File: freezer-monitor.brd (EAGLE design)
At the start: 50.8 x 22.9 mm, 7 parts, among them J1 1X2-3.5MM

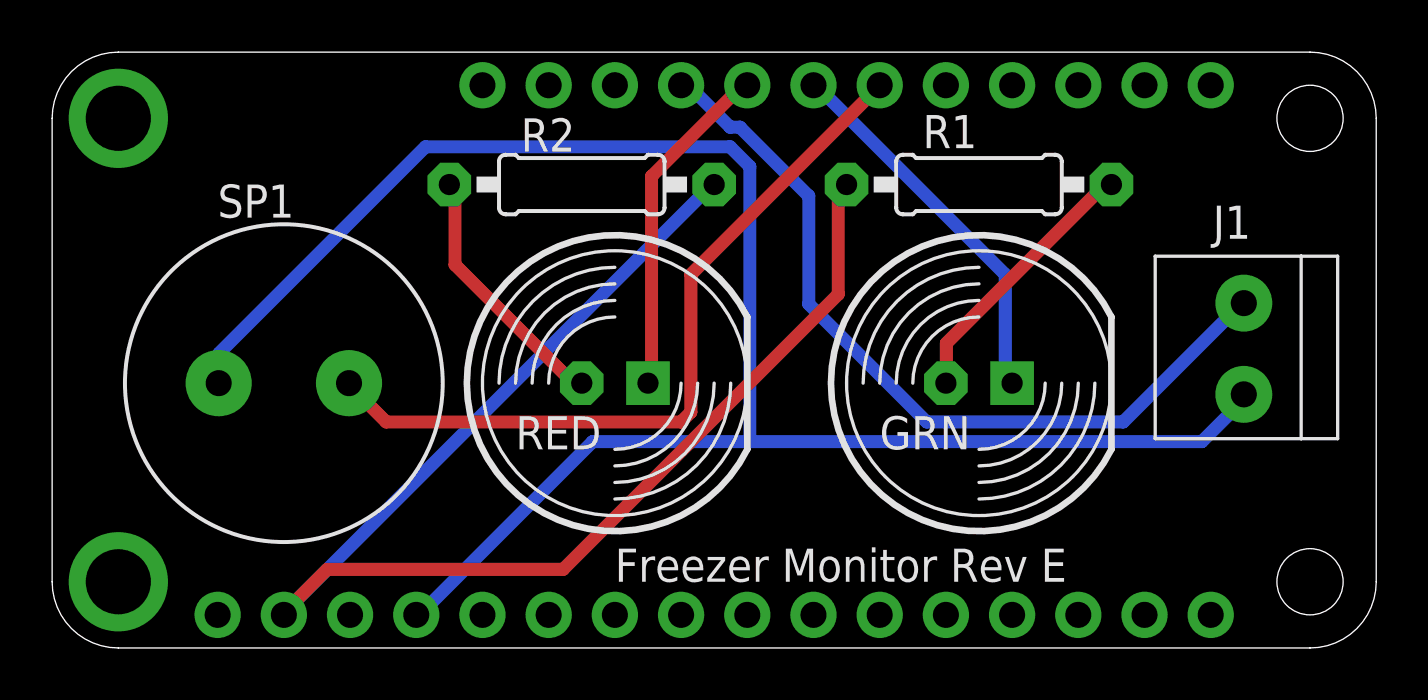
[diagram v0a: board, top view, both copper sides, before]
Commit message: Add line from USB to logic in
Update to bring power from USB port to logic in.  This so we can add the ability to text when the power is out.
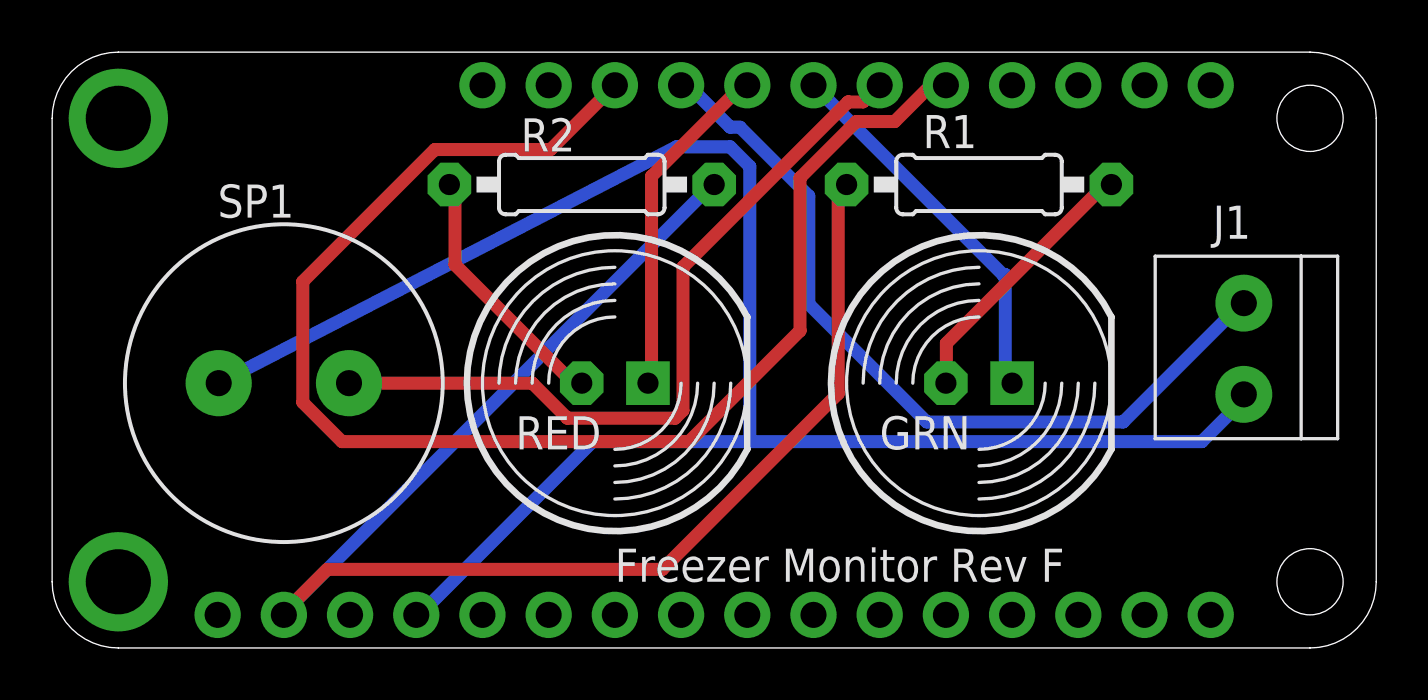
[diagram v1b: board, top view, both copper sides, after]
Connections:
- new net USB: MS1.21, MS1.26
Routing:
- net USB: track 0.00 -> 54.1 mm
- net GND: track 72.1 -> 68.8 mm
- net 3V: track 54.2 -> 56.5 mm
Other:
- board text added: "Freezer Monitor Rev F"
- board text removed: "Freezer Monitor Rev E"
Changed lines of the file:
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@@
 <?xml version="1.0" encoding="utf-8"?>
 <!DOCTYPE eagle SYSTEM "eagle.dtd">
-<eagle version="8.2.2">
+<eagle version="9.1.3">
 <drawing>
 <settings>
-<setting alwaysvectorfont="no"/>
+<setting alwaysvectorfont="yes"/>
+<setting keepoldvectorfont="yes"/>
 <setting verticaltext="up"/>
 </settings>
@@
 <board>
 <plain>
-<text x="21.59" y="2.54" size="1.27" layer="25">Freezer Monitor Rev E</text>
+<text x="21.59" y="2.54" size="1.27" layer="25">Freezer Monitor Rev F</text>
 </plain>
 <attributes>
@@
 <param name="dpMaxLengthDifference" value="10mm"/>
 <param name="dpGapFactor" value="2.5"/>
-<param name="checkGrid" value="0"/>
 <param name="checkAngle" value="0"/>
 <param name="checkFont" value="1"/>
 <param name="checkRestrict" value="1"/>
+<param name="checkStop" value="0"/>
+<param name="checkValues" value="0"/>
+<param name="checkNames" value="1"/>
+<param name="checkWireStubs" value="1"/>
+<param name="checkPolygonWidth" value="0"/>
 <param name="useDiameter" value="13"/>
 <param name="maxErrors" value="50"/>
@@
 <contactref element="MS1" pad="4"/>
 <contactref element="SP1" pad="P$1"/>
-<wire x1="6.5532" y1="11.303" x2="6.39" y2="10.16" width="0.3048" layer="16"/>
 <contactref element="J1" pad="2"/>
 <wire x1="20.735" y1="7.917" x2="14.326" y2="1.508" width="0.5" layer="16"/>
@@
 <wire x1="14.326" y1="1.508" x2="13.97" y2="1.27" width="0.5" layer="16"/>
 <wire x1="45.617" y1="9.425" x2="45.72" y2="9.73" width="0.5" layer="16"/>
-<wire x1="14.326" y1="19.227" x2="6.409" y2="11.31" width="0.5" layer="16"/>
-<wire x1="26.013" y1="19.227" x2="14.326" y2="19.227" width="0.5" layer="16"/>
 <wire x1="26.767" y1="18.473" x2="26.013" y2="19.227" width="0.5" layer="16"/>
 <wire x1="26.767" y1="7.917" x2="26.767" y2="18.473" width="0.5" layer="16"/>
-<wire x1="6.409" y1="11.31" x2="6.39" y2="10.16" width="0.5" layer="16"/>
+<wire x1="23.953" y1="19.227" x2="26.013" y2="19.227" width="0.5" layer="16"/>
+<wire x1="6.39" y1="10.16" x2="23.953" y2="19.227" width="0.5" layer="16"/>
 </signal>
 <signal name="N$3">
@@
 <signal name="N$6">
 <contactref element="MS1" pad="22"/>
+<wire x1="31.668" y1="21.489" x2="31.75" y2="21.59" width="0.5" layer="1"/>
 <contactref element="SP1" pad="P$2"/>
-<wire x1="24.505" y1="14.326" x2="31.668" y2="21.489" width="0.5" layer="1"/>
-<wire x1="24.505" y1="9.048" x2="24.505" y2="14.326" width="0.5" layer="1"/>
-<wire x1="24.128" y1="8.671" x2="24.505" y2="9.048" width="0.5" layer="1"/>
-<wire x1="12.818" y1="8.671" x2="24.128" y2="8.671" width="0.5" layer="1"/>
-<wire x1="11.687" y1="9.802" x2="12.818" y2="8.671" width="0.5" layer="1"/>
-<wire x1="31.668" y1="21.489" x2="31.75" y2="21.59" width="0.5" layer="1"/>
-<wire x1="11.687" y1="9.802" x2="11.39" y2="10.16" width="0.5" layer="1"/>
+<wire x1="31.75" y1="21.59" x2="31.111" y2="20.951" width="0.5" layer="1"/>
+<wire x1="31.111" y1="20.951" x2="30.541" y2="20.951" width="0.5" layer="1"/>
+<wire x1="24.2022" y1="9.1130375" x2="23.9069625" y2="8.8178" width="0.5" layer="1"/>
+<wire x1="23.9069625" y1="8.8178" x2="19.7640375" y2="8.8178" width="0.5" layer="1"/>
+<wire x1="18.4218375" y1="10.16" x2="11.39" y2="10.16" width="0.5" layer="1"/>
+<wire x1="19.7640375" y1="8.8178" x2="18.4218375" y2="10.16" width="0.5" layer="1"/>
+<wire x1="30.541" y1="20.951" x2="24.2022" y2="14.6122" width="0.5" layer="1"/>
+<wire x1="24.2022" y1="14.6122" x2="24.2022" y2="9.1130375" width="0.5" layer="1"/>
 </signal>
 <signal name="N$5">
@@
 <contactref element="GRN" pad="K"/>
 <wire x1="36.569" y1="14.326" x2="36.569" y2="10.179" width="0.5" layer="16"/>
-<wire x1="29.406" y1="21.489" x2="36.569" y2="14.326" width="0.5" layer="16"/>
 <wire x1="36.569" y1="10.179" x2="36.83" y2="10.16" width="0.5" layer="16"/>
-<wire x1="29.406" y1="21.489" x2="29.21" y2="21.59" width="0.5" layer="16"/>
+<wire x1="29.21" y1="21.59" x2="36.474" y2="14.326" width="0.5" layer="16"/>
+<wire x1="36.474" y1="14.326" x2="36.569" y2="14.326" width="0.5" layer="16"/>
 </signal>
 <signal name="3V">
@@
 <wire x1="25.259" y1="17.719" x2="25.4" y2="17.78" width="0.5" layer="16"/>
 <wire x1="9.048" y1="1.508" x2="8.89" y2="1.27" width="0.5" layer="16"/>
-<wire x1="30.16" y1="13.572" x2="30.16" y2="17.719" width="0.5" layer="1"/>
-<wire x1="19.604" y1="3.016" x2="30.16" y2="13.572" width="0.5" layer="1"/>
-<wire x1="10.556" y1="3.016" x2="19.604" y2="3.016" width="0.5" layer="1"/>
+<wire x1="30.16" y1="9.762" x2="30.16" y2="17.719" width="0.5" layer="1"/>
+<wire x1="23.414" y1="3.016" x2="30.16" y2="9.762" width="0.5" layer="1"/>
+<wire x1="10.556" y1="3.016" x2="23.414" y2="3.016" width="0.5" layer="1"/>
 <wire x1="9.048" y1="1.508" x2="10.556" y2="3.016" width="0.5" layer="1"/>
 <wire x1="30.16" y1="17.719" x2="30.48" y2="17.78" width="0.5" layer="1"/>
@@
 <wire x1="19.981" y1="10.179" x2="20.32" y2="10.16" width="0.5" layer="1"/>
 </signal>
+<signal name="USB">
+<contactref element="MS1" pad="26"/>
+<contactref element="MS1" pad="21"/>
+<wire x1="34.29" y1="21.59" x2="33.72" y2="21.59" width="0.5" layer="1"/>
+<wire x1="33.72" y1="21.59" x2="32.327" y2="20.197" width="0.5" layer="1"/>
+<wire x1="32.327" y1="20.197" x2="30.85331875" y2="20.197" width="0.5" layer="1"/>
+<wire x1="30.85331875" y1="20.197" x2="28.694" y2="18.03768125" width="0.5" layer="1"/>
+<wire x1="28.694" y1="18.03768125" x2="28.694" y2="12.17068125" width="0.5" layer="1"/>
+<wire x1="28.694" y1="12.17068125" x2="24.44031875" y2="7.917" width="0.5" layer="1"/>
+<wire x1="24.44031875" y1="7.917" x2="11.12418125" y2="7.917" width="0.5" layer="1"/>
+<wire x1="11.12418125" y1="7.917" x2="9.616" y2="9.42518125" width="0.5" layer="1"/>
+<wire x1="14.6840375" y1="19.1222" x2="19.1222" y2="19.1222" width="0.5" layer="1"/>
+<wire x1="19.1222" y1="19.1222" x2="21.59" y2="21.59" width="0.5" layer="1"/>
+<wire x1="9.616" y1="9.42518125" x2="9.616" y2="14.0541625" width="0.5" layer="1"/>
+<wire x1="9.616" y1="14.0541625" x2="14.6840375" y2="19.1222" width="0.5" layer="1"/>
+</signal>
 </signals>
+<mfgpreviewcolors>
+<mfgpreviewcolor name="soldermaskcolor" color="0xC8008000"/>
+<mfgpreviewcolor name="silkscreencolor" color="0xFFFEFEFE"/>
+<mfgpreviewcolor name="backgroundcolor" color="0xFF282828"/>
+<mfgpreviewcolor name="coppercolor" color="0xFFFFBF00"/>
+<mfgpreviewcolor name="substratecolor" color="0xFF786E46"/>
+</mfgpreviewcolors>
 </board>
 </drawing>
 <compatibility>
 <note version="8.2" severity="warning">
-Since Version 8.2, Eagle supports online libraries. The ids
+Since Version 8.2, EAGLE supports online libraries. The ids
 of those online libraries will not be understood (or retained)
 with this version.

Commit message: Revert "Add line from USB to logic in"
This reverts commit aa022d101621f46ab4c7c753449e8c0f6e997a72.
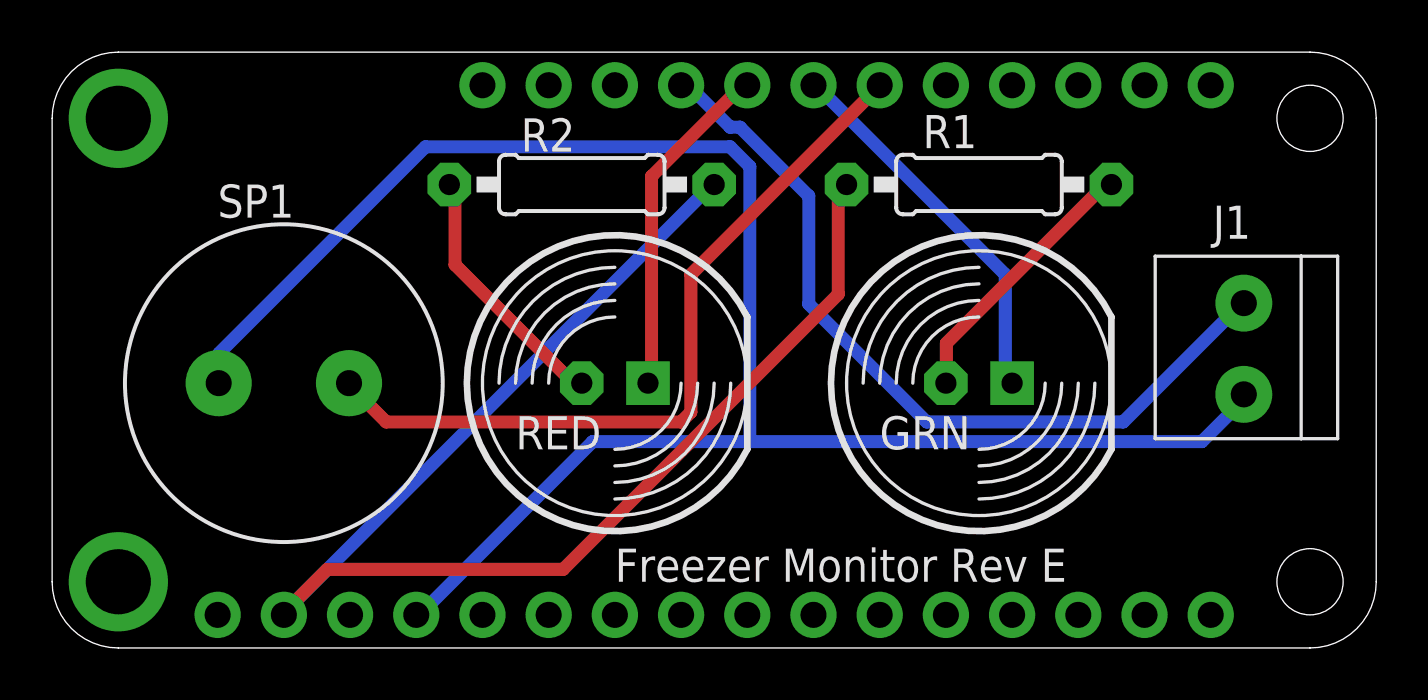
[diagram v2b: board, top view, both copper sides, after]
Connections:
- removed net USB: MS1.21, MS1.26
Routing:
- net USB: track 54.1 -> 0.00 mm
- net GND: track 68.8 -> 72.1 mm
- net 3V: track 56.5 -> 54.2 mm
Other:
- board text added: "Freezer Monitor Rev E"
- board text removed: "Freezer Monitor Rev F"
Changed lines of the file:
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@@
 <?xml version="1.0" encoding="utf-8"?>
 <!DOCTYPE eagle SYSTEM "eagle.dtd">
-<eagle version="9.1.3">
+<eagle version="8.2.2">
 <drawing>
 <settings>
-<setting alwaysvectorfont="yes"/>
-<setting keepoldvectorfont="yes"/>
+<setting alwaysvectorfont="no"/>
 <setting verticaltext="up"/>
 </settings>
@@
 <board>
 <plain>
-<text x="21.59" y="2.54" size="1.27" layer="25">Freezer Monitor Rev F</text>
+<text x="21.59" y="2.54" size="1.27" layer="25">Freezer Monitor Rev E</text>
 </plain>
 <attributes>
@@
 <param name="dpMaxLengthDifference" value="10mm"/>
 <param name="dpGapFactor" value="2.5"/>
+<param name="checkGrid" value="0"/>
 <param name="checkAngle" value="0"/>
 <param name="checkFont" value="1"/>
 <param name="checkRestrict" value="1"/>
-<param name="checkStop" value="0"/>
-<param name="checkValues" value="0"/>
-<param name="checkNames" value="1"/>
-<param name="checkWireStubs" value="1"/>
-<param name="checkPolygonWidth" value="0"/>
 <param name="useDiameter" value="13"/>
 <param name="maxErrors" value="50"/>
@@
 <contactref element="MS1" pad="4"/>
 <contactref element="SP1" pad="P$1"/>
+<wire x1="6.5532" y1="11.303" x2="6.39" y2="10.16" width="0.3048" layer="16"/>
 <contactref element="J1" pad="2"/>
 <wire x1="20.735" y1="7.917" x2="14.326" y2="1.508" width="0.5" layer="16"/>
@@
 <wire x1="14.326" y1="1.508" x2="13.97" y2="1.27" width="0.5" layer="16"/>
 <wire x1="45.617" y1="9.425" x2="45.72" y2="9.73" width="0.5" layer="16"/>
+<wire x1="14.326" y1="19.227" x2="6.409" y2="11.31" width="0.5" layer="16"/>
+<wire x1="26.013" y1="19.227" x2="14.326" y2="19.227" width="0.5" layer="16"/>
 <wire x1="26.767" y1="18.473" x2="26.013" y2="19.227" width="0.5" layer="16"/>
 <wire x1="26.767" y1="7.917" x2="26.767" y2="18.473" width="0.5" layer="16"/>
-<wire x1="23.953" y1="19.227" x2="26.013" y2="19.227" width="0.5" layer="16"/>
-<wire x1="6.39" y1="10.16" x2="23.953" y2="19.227" width="0.5" layer="16"/>
+<wire x1="6.409" y1="11.31" x2="6.39" y2="10.16" width="0.5" layer="16"/>
 </signal>
 <signal name="N$3">
@@
 <signal name="N$6">
 <contactref element="MS1" pad="22"/>
+<contactref element="SP1" pad="P$2"/>
+<wire x1="24.505" y1="14.326" x2="31.668" y2="21.489" width="0.5" layer="1"/>
+<wire x1="24.505" y1="9.048" x2="24.505" y2="14.326" width="0.5" layer="1"/>
+<wire x1="24.128" y1="8.671" x2="24.505" y2="9.048" width="0.5" layer="1"/>
+<wire x1="12.818" y1="8.671" x2="24.128" y2="8.671" width="0.5" layer="1"/>
+<wire x1="11.687" y1="9.802" x2="12.818" y2="8.671" width="0.5" layer="1"/>
 <wire x1="31.668" y1="21.489" x2="31.75" y2="21.59" width="0.5" layer="1"/>
-<contactref element="SP1" pad="P$2"/>
-<wire x1="31.75" y1="21.59" x2="31.111" y2="20.951" width="0.5" layer="1"/>
-<wire x1="31.111" y1="20.951" x2="30.541" y2="20.951" width="0.5" layer="1"/>
-<wire x1="24.2022" y1="9.1130375" x2="23.9069625" y2="8.8178" width="0.5" layer="1"/>
-<wire x1="23.9069625" y1="8.8178" x2="19.7640375" y2="8.8178" width="0.5" layer="1"/>
-<wire x1="18.4218375" y1="10.16" x2="11.39" y2="10.16" width="0.5" layer="1"/>
-<wire x1="19.7640375" y1="8.8178" x2="18.4218375" y2="10.16" width="0.5" layer="1"/>
-<wire x1="30.541" y1="20.951" x2="24.2022" y2="14.6122" width="0.5" layer="1"/>
-<wire x1="24.2022" y1="14.6122" x2="24.2022" y2="9.1130375" width="0.5" layer="1"/>
+<wire x1="11.687" y1="9.802" x2="11.39" y2="10.16" width="0.5" layer="1"/>
 </signal>
 <signal name="N$5">
@@
 <contactref element="GRN" pad="K"/>
 <wire x1="36.569" y1="14.326" x2="36.569" y2="10.179" width="0.5" layer="16"/>
+<wire x1="29.406" y1="21.489" x2="36.569" y2="14.326" width="0.5" layer="16"/>
 <wire x1="36.569" y1="10.179" x2="36.83" y2="10.16" width="0.5" layer="16"/>
-<wire x1="29.21" y1="21.59" x2="36.474" y2="14.326" width="0.5" layer="16"/>
-<wire x1="36.474" y1="14.326" x2="36.569" y2="14.326" width="0.5" layer="16"/>
+<wire x1="29.406" y1="21.489" x2="29.21" y2="21.59" width="0.5" layer="16"/>
 </signal>
 <signal name="3V">
@@
 <wire x1="25.259" y1="17.719" x2="25.4" y2="17.78" width="0.5" layer="16"/>
 <wire x1="9.048" y1="1.508" x2="8.89" y2="1.27" width="0.5" layer="16"/>
-<wire x1="30.16" y1="9.762" x2="30.16" y2="17.719" width="0.5" layer="1"/>
-<wire x1="23.414" y1="3.016" x2="30.16" y2="9.762" width="0.5" layer="1"/>
-<wire x1="10.556" y1="3.016" x2="23.414" y2="3.016" width="0.5" layer="1"/>
+<wire x1="30.16" y1="13.572" x2="30.16" y2="17.719" width="0.5" layer="1"/>
+<wire x1="19.604" y1="3.016" x2="30.16" y2="13.572" width="0.5" layer="1"/>
+<wire x1="10.556" y1="3.016" x2="19.604" y2="3.016" width="0.5" layer="1"/>
 <wire x1="9.048" y1="1.508" x2="10.556" y2="3.016" width="0.5" layer="1"/>
 <wire x1="30.16" y1="17.719" x2="30.48" y2="17.78" width="0.5" layer="1"/>
@@
 <wire x1="19.981" y1="10.179" x2="20.32" y2="10.16" width="0.5" layer="1"/>
 </signal>
-<signal name="USB">
-<contactref element="MS1" pad="26"/>
-<contactref element="MS1" pad="21"/>
-<wire x1="34.29" y1="21.59" x2="33.72" y2="21.59" width="0.5" layer="1"/>
-<wire x1="33.72" y1="21.59" x2="32.327" y2="20.197" width="0.5" layer="1"/>
-<wire x1="32.327" y1="20.197" x2="30.85331875" y2="20.197" width="0.5" layer="1"/>
-<wire x1="30.85331875" y1="20.197" x2="28.694" y2="18.03768125" width="0.5" layer="1"/>
-<wire x1="28.694" y1="18.03768125" x2="28.694" y2="12.17068125" width="0.5" layer="1"/>
-<wire x1="28.694" y1="12.17068125" x2="24.44031875" y2="7.917" width="0.5" layer="1"/>
-<wire x1="24.44031875" y1="7.917" x2="11.12418125" y2="7.917" width="0.5" layer="1"/>
-<wire x1="11.12418125" y1="7.917" x2="9.616" y2="9.42518125" width="0.5" layer="1"/>
-<wire x1="14.6840375" y1="19.1222" x2="19.1222" y2="19.1222" width="0.5" layer="1"/>
-<wire x1="19.1222" y1="19.1222" x2="21.59" y2="21.59" width="0.5" layer="1"/>
-<wire x1="9.616" y1="9.42518125" x2="9.616" y2="14.0541625" width="0.5" layer="1"/>
-<wire x1="9.616" y1="14.0541625" x2="14.6840375" y2="19.1222" width="0.5" layer="1"/>
-</signal>
 </signals>
-<mfgpreviewcolors>
-<mfgpreviewcolor name="soldermaskcolor" color="0xC8008000"/>
-<mfgpreviewcolor name="silkscreencolor" color="0xFFFEFEFE"/>
-<mfgpreviewcolor name="backgroundcolor" color="0xFF282828"/>
-<mfgpreviewcolor name="coppercolor" color="0xFFFFBF00"/>
-<mfgpreviewcolor name="substratecolor" color="0xFF786E46"/>
-</mfgpreviewcolors>
 </board>
 </drawing>
 <compatibility>
 <note version="8.2" severity="warning">
-Since Version 8.2, EAGLE supports online libraries. The ids
+Since Version 8.2, Eagle supports online libraries. The ids
 of those online libraries will not be understood (or retained)
 with this version.
